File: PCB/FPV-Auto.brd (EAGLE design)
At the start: 65.5 x 30 mm, 93 parts, among them Q310 CSD25402Q3A, Q320 BSS138, U110 NRF24L01+_MINI, U120 74LVC2T45DCT, U140 DRV8835, U200 RASPBERRY_PI_ZERO_W_V1.1_GPIO, U210 MAX98357A, U300 BQ25892, U330 TPS61236P, U340 TPS61236P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

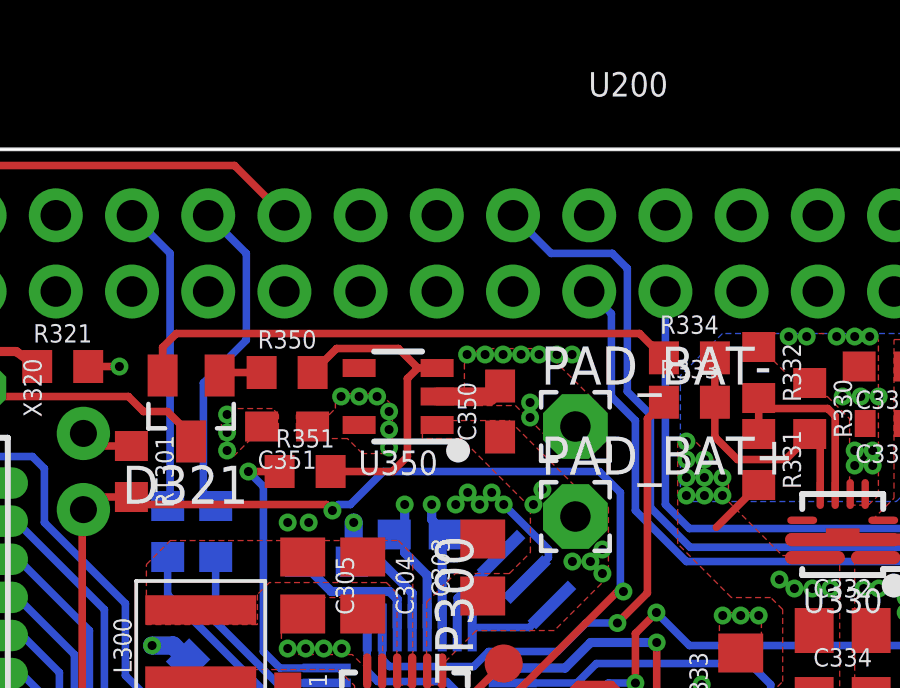
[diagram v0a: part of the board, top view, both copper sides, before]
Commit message: Changes on Raspberry GPIO assignment
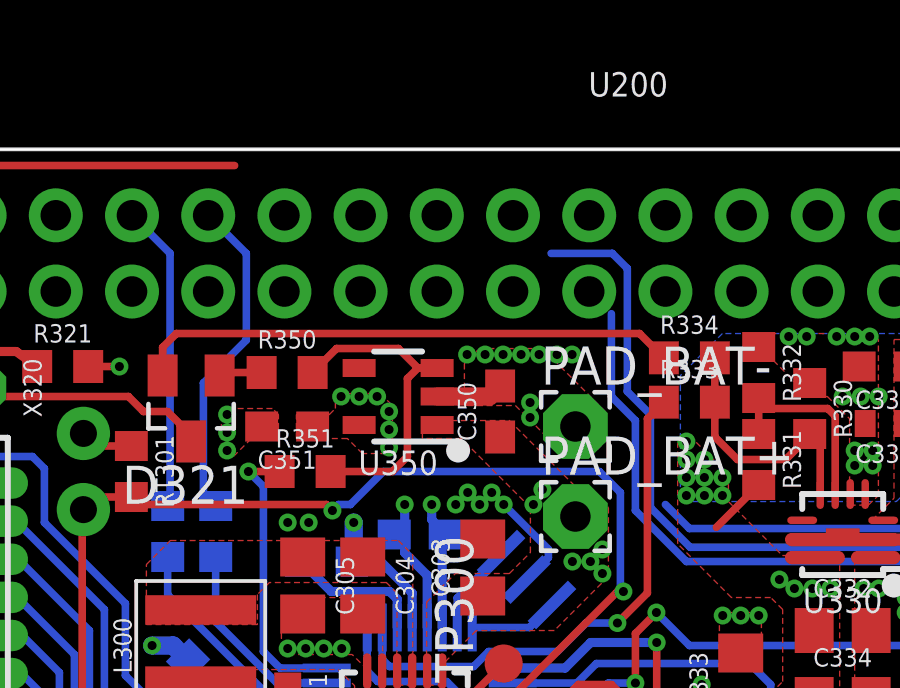
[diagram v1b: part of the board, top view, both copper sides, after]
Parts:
- C212, C213: value 680pF -> 220pF
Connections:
- net BCLK: now also U200.12; no longer U200.18
- net DIN: now also U200.40; no longer U200.21
- net LRCLK: now also U200.35; no longer U200.19
- net RASPI_DTR: now also U200.15; no longer U200.12
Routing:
- net DIN: track 20.1 -> 13.0 mm
- net RASPI_DTR: track 29.6 -> 27.3 mm
- net BCLK: track 30.0 -> 28.2 mm
- net LRCLK: track 26.8 -> 25.7 mm
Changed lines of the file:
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@@
 <grid distance="1" unitdist="mm" unit="mm" style="lines" multiple="1" display="no" altdistance="0.1" altunitdist="mm" altunit="mm"/>
 <layers>
-<layer number="1" name="Top" color="4" fill="1" visible="yes" active="yes"/>
+<layer number="1" name="Top" color="4" fill="1" visible="no" active="yes"/>
 <layer number="2" name="Route2" color="1" fill="3" visible="no" active="yes"/>
 <layer number="3" name="Route3" color="4" fill="3" visible="no" active="no"/>
@@
 <layer number="19" name="Unrouted" color="6" fill="1" visible="yes" active="yes"/>
 <layer number="20" name="Dimension" color="15" fill="1" visible="yes" active="yes"/>
-<layer number="21" name="tPlace" color="7" fill="1" visible="yes" active="yes"/>
+<layer number="21" name="tPlace" color="7" fill="1" visible="no" active="yes"/>
 <layer number="22" name="bPlace" color="7" fill="1" visible="yes" active="yes"/>
 <layer number="23" name="tOrigins" color="15" fill="1" visible="yes" active="yes"/>
@@
 <layer number="49" name="Reference" color="7" fill="1" visible="no" active="yes"/>
 <layer number="50" name="dxf" color="7" fill="1" visible="no" active="no"/>
-<layer number="51" name="tDocu" color="7" fill="1" visible="yes" active="yes"/>
+<layer number="51" name="tDocu" color="7" fill="1" visible="no" active="yes"/>
 <layer number="52" name="bDocu" color="7" fill="1" visible="yes" active="yes"/>
 <layer number="53" name="tGND_GNDA" color="7" fill="1" visible="no" active="no"/>
@@
 <element name="R200" library="FPV-Auto" package="R0603" value="1K" x="17.69" y="17.26" rot="MR270"/>
 <element name="R201" library="FPV-Auto" package="R0603" value="1K" x="19.29" y="17.26" rot="MR270"/>
-<element name="C212" library="FPV-Auto" package="C0603" value="680pF" x="55.99" y="18.36" rot="MR270"/>
-<element name="C213" library="FPV-Auto" package="C0603" value="680pF" x="55.99" y="22.46" rot="MR90"/>
+<element name="C212" library="FPV-Auto" package="C0603" value="220pF" x="55.99" y="18.36" rot="MR270"/>
+<element name="C213" library="FPV-Auto" package="C0603" value="220pF" x="55.99" y="22.46" rot="MR90"/>
 <element name="R211" library="FPV-Auto" package="R0603_SWITCH_2_WAY" value="R_SWITCH_2_WAY_0603" x="44.19" y="18.46" rot="MR180"/>
 <element name="FB210" library="FPV-Auto" package="0603" value="BLM18SG331TN1" x="54.38" y="20.77" rot="MR90">
@@
 </signal>
 <signal name="BCLK">
-<contactref element="U200" pad="18"/>
 <contactref element="U210" pad="16"/>
 <wire x1="30.47" y1="26.53" x2="32.51" y2="26.53" width="0.254" layer="16"/>
 <wire x1="47.74" y1="16.31" x2="47.74" y2="16.735" width="0.254" layer="16"/>
 <wire x1="33.01" y1="26.03" x2="32.51" y2="26.53" width="0.254" layer="16"/>
-<wire x1="30.47" y1="26.53" x2="29.2" y2="27.8" width="0.254" layer="16"/>
 <wire x1="47.74" y1="16.02" x2="47.74" y2="16.735" width="0.254" layer="16"/>
 <wire x1="33.01" y1="26.03" x2="33.01" y2="21.93" width="0.254" layer="16"/>
@@
 <wire x1="44.58" y1="14.56" x2="46.28" y2="14.56" width="0.254" layer="16"/>
 <wire x1="46.28" y1="14.56" x2="47.74" y2="16.02" width="0.254" layer="16"/>
+<contactref element="U200" pad="12"/>
+<wire x1="21.58" y1="27.8" x2="30.47" y2="26.53" width="0" layer="19" extent="16-16"/>
 </signal>
 <signal name="LRCLK">
-<contactref element="U200" pad="19"/>
 <contactref element="U210" pad="14"/>
 <wire x1="48.74" y1="15.61" x2="48.74" y2="16.735" width="0.254" layer="16"/>
@@
 <wire x1="44.38" y1="14.06" x2="47.19" y2="14.06" width="0.254" layer="16"/>
 <wire x1="47.19" y1="14.06" x2="48.74" y2="15.61" width="0.254" layer="16"/>
-<wire x1="31.74" y1="25.26" x2="32.48" y2="24.52" width="0.254" layer="16"/>
 <wire x1="32.48" y1="24.52" x2="32.48" y2="21.76" width="0.254" layer="16"/>
 <wire x1="32.48" y1="21.76" x2="33.28" y2="20.96" width="0.254" layer="16"/>
+<contactref element="U200" pad="35"/>
+<wire x1="48.74" y1="16.735" x2="52.06" y2="25.26" width="0" layer="19" extent="16-16"/>
 </signal>
 <signal name="DIN">
-<contactref element="U200" pad="21"/>
 <contactref element="U210" pad="1"/>
 <wire x1="42.83" y1="17.61" x2="46.865" y2="17.61" width="0.254" layer="16"/>
-<wire x1="34.28" y1="25.26" x2="34.28" y2="18.16" width="0.254" layer="16"/>
 <wire x1="34.28" y1="18.16" x2="35.08" y2="17.36" width="0.254" layer="16"/>
 <wire x1="35.08" y1="17.36" x2="42.58" y2="17.36" width="0.254" layer="16"/>
 <wire x1="42.58" y1="17.36" x2="42.83" y2="17.61" width="0.254" layer="16"/>
+<contactref element="U200" pad="40"/>
+<wire x1="46.865" y1="17.61" x2="57.14" y2="27.8" width="0" layer="19" extent="16-16"/>
 </signal>
 <signal name="GAIN">
@@
 </signal>
 <signal name="RASPI_DTR">
-<contactref element="U200" pad="12"/>
 <contactref element="Q320" pad="2"/>
 <wire x1="2.34" y1="17.56" x2="2.34" y2="18.81" width="0.254" layer="1"/>
@@
 <wire x1="7.49" y1="28.66" x2="8.29" y2="29.46" width="0.254" layer="1"/>
 <wire x1="8.29" y1="29.46" x2="19.92" y2="29.46" width="0.254" layer="1"/>
-<wire x1="19.92" y1="29.46" x2="21.58" y2="27.8" width="0.254" layer="1"/>
+<contactref element="U200" pad="15"/>
+<wire x1="19.92" y1="29.46" x2="26.66" y2="25.26" width="0" layer="19" extent="1-1"/>
 </signal>
 <signal name="AOUT1">

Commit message: Update PCB Layout
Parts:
- added R101: 10K, FPV-Auto:R0603
- added R103: 1K, FPV-Auto:R0603
- R102: value 10K -> 1K
- moved R102 7.48 mm to (20.0, 4.95), flipped to the top, turned to 225 degrees
- moved R300 0.60 mm to (16.8, 2.15)
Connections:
- net +3V3: now also R101.2, R103.2
- net GND: now also U110.9
- net RESET: now also R101.1; no longer R102.1
- net SCL: now also R103.1
- net SDA: now also R102.1
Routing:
- net DIN: track 13.0 -> 46.3 mm
- net LRCLK: track 25.7 -> 14.9 mm, vias 0 -> 1
- net RASPI_DTR: track 27.3 -> 37.2 mm
- net BCLK: track 28.2 -> 37.6 mm
- net RESET: track 45.8 -> 48.4 mm
- net +3V3: track 23.4 -> 25.9 mm, vias 14 -> 15
- net STAT: track 11.1 -> 11.7 mm
- net SDA: track 17.9 -> 18.4 mm
- net SCL: track 15.9 -> 16.5 mm
- net N$19: track 3.99 -> 3.48 mm
- net BAT: vias 21 -> 22

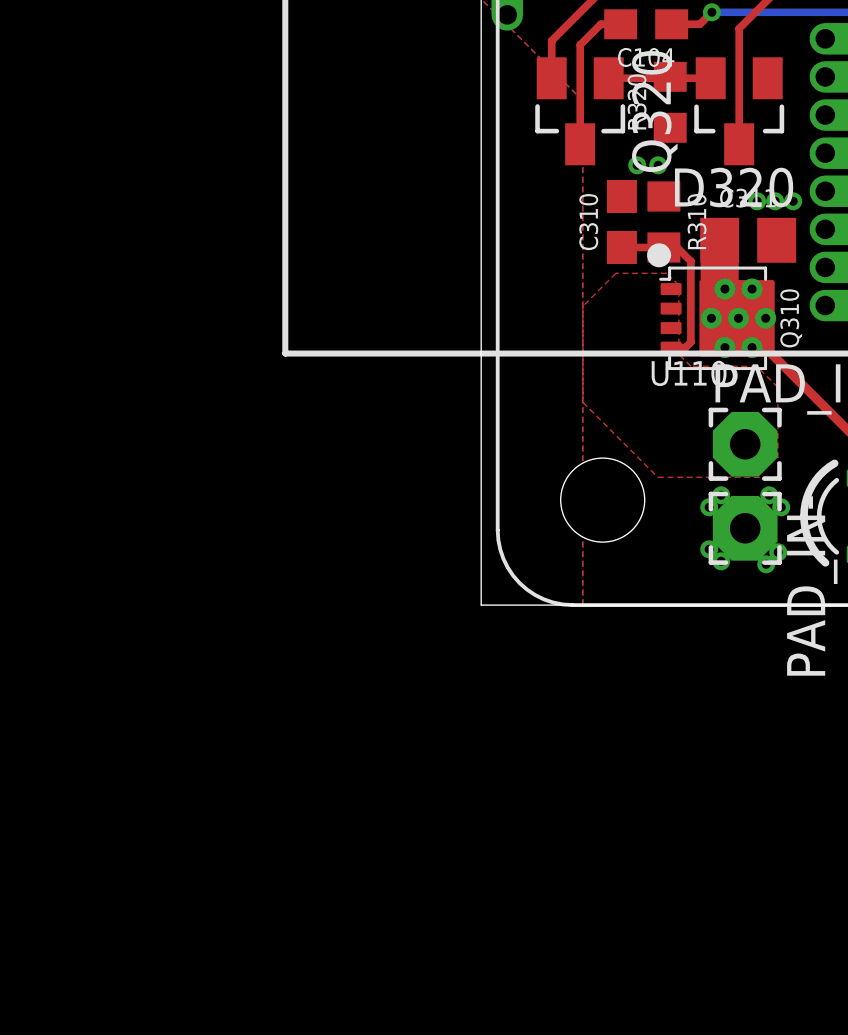
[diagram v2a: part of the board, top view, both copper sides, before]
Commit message: Z-Diode on reverse-prot-mosfet, button also on AVR, other minor changes
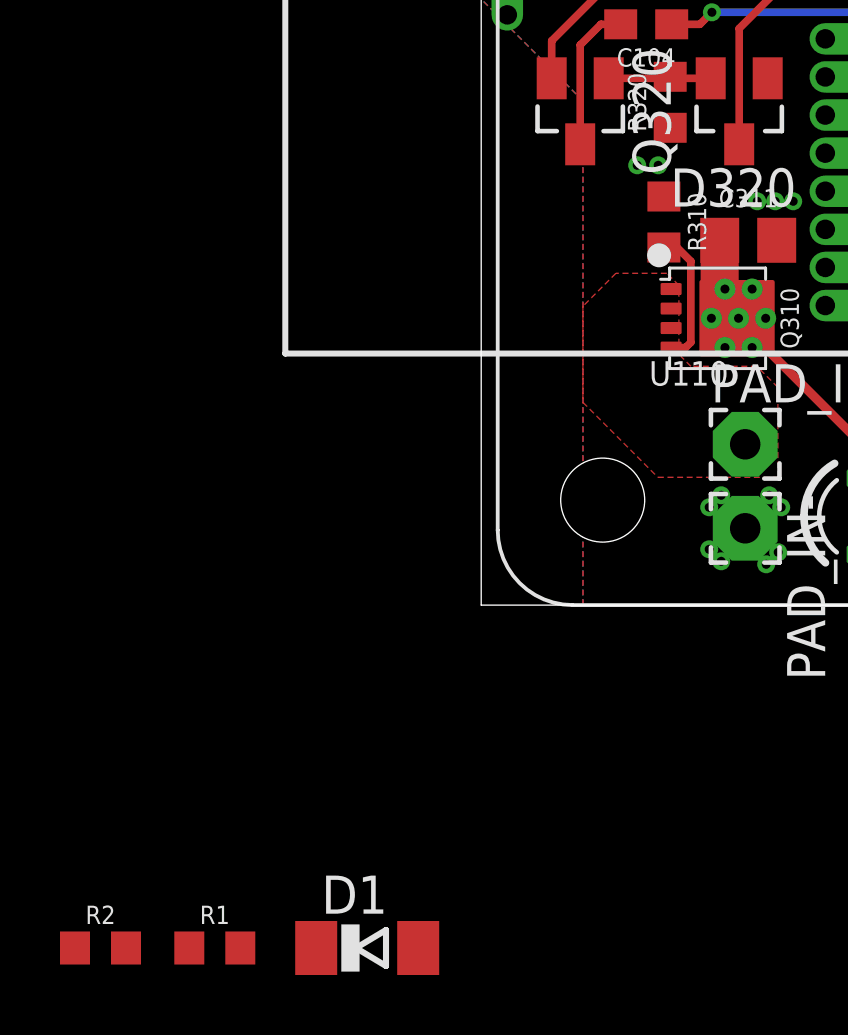
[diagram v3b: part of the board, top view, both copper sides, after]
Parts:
- removed C310: (no value), FPV-Auto:C0603
- added D1: (no value), diode:SOD80C
- added R1, R2: 100K, FPV-Auto:R0603
- R102, R103: value 1K -> 10K
- R310: value 100K -> 10K
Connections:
- new net BUTTON_SENSE: R1.1, R2.2, U100.19
- new net N$15: D320.1, R1.2
- net GND: now also R2.1; no longer C310.2
- net N$16: now also D1.A; no longer C310.1
- net VBUS: now also D1.C
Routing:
- net N$16: track 5.92 -> 4.52 mm

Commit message: updated lib and pcb
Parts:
- removed D1: (no value), diode:SOD80C
- removed R1, R2: 100K, FPV-Auto:R0603
- added D310: BZX585-B9V1, FPV-Auto:SOD523(SC-79)
- added R322, R323: 100K, FPV-Auto:R0603
- U100: value (none) -> ATMEGA328P-AU
- U200: device FPV-Auto:RASPBERRY_PI_ZERO_W_V1.1 -> FPV-Auto:RASPBERRY_PI_ZERO_W_V1.1_GPIO
- moved C311 0.34 mm to (8.91, 12.5)
- moved R310 0.07 mm to (6.10, 12.7)
- flipped U110 to the bottom, turned to 270 degrees
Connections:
- removed net NRF_MISO: U100.26, U110.7
- removed net SCK/NRF_CE: U100.17, U110.3, X100.3
- new net NRF_CE: U100.26, U110.3
- new net SCK/NRF_MISO: U100.17, U110.7, X100.3
- net BUTTON_SENSE: now also R322.1, R323.2, U100.22; no longer R1.1, R2.2, U100.19
- net GND: now also R323.1; no longer R2.1
- net N$15: now also R322.2; no longer R1.2
- net N$16: now also D310.A; no longer D1.A
- net NRF_!CS: now also U100.25; no longer U100.23
- net NRF_MOSI: now also U100.23; no longer U100.25
- net VBUS: now also D310.C; no longer D1.C
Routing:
- net SCK/NRF_MISO: track 0.00 -> 30.5 mm
- net SCK/NRF_CE: track 30.2 -> 0.00 mm
- net NRF_MISO: track 22.1 -> 0.00 mm
- net NRF_CE: track 0.00 -> 20.8 mm
- net N$15: track 0.00 -> 18.7 mm, vias 0 -> 1
- net BUTTON_SENSE: track 0.00 -> 12.4 mm
- net VBUS: track 11.4 -> 16.5 mm
- net N$16: track 4.52 -> 6.59 mm
- net NRF_!CS: track 21.7 -> 20.0 mm
- net NRF_SCK: track 21.2 -> 20.0 mm
- net GND: track 43.7 -> 44.6 mm, vias 109 -> 108
- net NRF_MOSI: track 21.2 -> 20.4 mm

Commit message: Kommentare...
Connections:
- removed net STAT: R300.1, U300.4
- new net N$20: LED300.A, LED301.A, R300.1
- net N$19: now also U300.4; no longer R300.2
- net VBUS: now also R300.2; no longer LED300.A, LED301.A
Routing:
- net STAT: track 12.0 -> 0.00 mm, vias 2 -> 0
- net VBUS: track 16.5 -> 13.5 mm
- net N$20: track 0.00 -> 2.03 mm
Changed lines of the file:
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@@
 <layers>
 <layer number="1" name="Top" color="4" fill="1" visible="yes" active="yes"/>
-<layer number="2" name="Route2" color="1" fill="3" visible="no" active="yes"/>
+<layer number="2" name="Route2" color="3" fill="1" visible="no" active="yes"/>
 <layer number="3" name="Route3" color="4" fill="3" visible="no" active="no"/>
 <layer number="14" name="Route14" color="1" fill="6" visible="no" active="no"/>
-<layer number="15" name="Route15" color="4" fill="6" visible="no" active="yes"/>
-<layer number="16" name="Bottom" color="1" fill="1" visible="yes" active="yes"/>
+<layer number="15" name="Route15" color="5" fill="1" visible="no" active="yes"/>
+<layer number="16" name="Bottom" color="1" fill="1" visible="no" active="yes"/>
 <layer number="17" name="Pads" color="2" fill="1" visible="yes" active="yes"/>
 <layer number="18" name="Vias" color="2" fill="1" visible="yes" active="yes"/>
@@
 <layer number="20" name="Dimension" color="15" fill="1" visible="yes" active="yes"/>
 <layer number="21" name="tPlace" color="7" fill="1" visible="yes" active="yes"/>
-<layer number="22" name="bPlace" color="7" fill="1" visible="yes" active="yes"/>
+<layer number="22" name="bPlace" color="7" fill="1" visible="no" active="yes"/>
 <layer number="23" name="tOrigins" color="15" fill="1" visible="yes" active="yes"/>
-<layer number="24" name="bOrigins" color="15" fill="1" visible="yes" active="yes"/>
+<layer number="24" name="bOrigins" color="15" fill="1" visible="no" active="yes"/>
 <layer number="25" name="tNames" color="7" fill="1" visible="no" active="yes"/>
 <layer number="26" name="bNames" color="7" fill="1" visible="no" active="yes"/>
 <layer number="27" name="tValues" color="7" fill="1" visible="no" active="yes"/>
 <layer number="28" name="bValues" color="7" fill="1" visible="no" active="yes"/>
-<layer number="29" name="tStop" color="7" fill="3" visible="no" active="yes"/>
+<layer number="29" name="tStop" color="7" fill="3" visible="yes" active="yes"/>
 <layer number="30" name="bStop" color="7" fill="6" visible="no" active="yes"/>
 <layer number="31" name="tCream" color="7" fill="4" visible="no" active="yes"/>
@@
 <layer number="50" name="dxf" color="7" fill="1" visible="no" active="no"/>
 <layer number="51" name="tDocu" color="7" fill="1" visible="yes" active="yes"/>
-<layer number="52" name="bDocu" color="7" fill="1" visible="yes" active="yes"/>
+<layer number="52" name="bDocu" color="7" fill="1" visible="no" active="yes"/>
 <layer number="53" name="tGND_GNDA" color="7" fill="1" visible="no" active="no"/>
 <layer number="54" name="bGND_GNDA" color="7" fill="1" visible="no" active="no"/>
@@
 <contactref element="Q310" pad="TP2" route="any" routetag="A.S"/>
 <contactref element="C311" pad="1"/>
-<contactref element="LED300" pad="A"/>
 <via x="23.7" y="8.6" extent="1-16" drill="0.3"/>
 <via x="23.7" y="8" extent="1-16" drill="0.3"/>
@@
 <via x="23.1" y="8" extent="1-16" drill="0.3"/>
 <via x="23.1" y="7.4" extent="1-16" drill="0.3"/>
-<contactref element="LED301" pad="A"/>
-<wire x1="12.8" y1="4.27" x2="13.32" y2="3.75" width="0.254" layer="1"/>
-<wire x1="13.32" y1="3.75" x2="14.61" y2="3.75" width="0.254" layer="1"/>
 <wire x1="7.96" y1="12.5" x2="7.96" y2="12" width="1.27" layer="1"/>
 <wire x1="7.96" y1="12" x2="7.96" y2="9.6" width="1.27" layer="1"/>
 <wire x1="7.96" y1="9.6" x2="8.5875" y2="9.6" width="1.27" layer="1"/>
-<wire x1="12.8" y1="4.27" x2="12.8" y2="5.3" width="0.3048" layer="1"/>
 <wire x1="12.8" y1="5.3" x2="9.475" y2="8.625" width="0.3048" layer="1"/>
 <wire x1="9.475" y1="8.625" x2="9.04" y2="8.625" width="0.3048" layer="1"/>
@@
 <wire x1="4.7" y1="12.7" x2="7.96" y2="12.7" width="0.254" layer="1"/>
 <wire x1="7.96" y1="12.7" x2="7.96" y2="12" width="0.254" layer="1"/>
+<contactref element="R300" pad="2"/>
+<wire x1="12.8" y1="5.3" x2="15.95" y2="2.19" width="0" layer="19" extent="1-1"/>
 </signal>
 <signal name="N$17">
@@
 </polygon>
 </signal>
-<signal name="STAT">
-<contactref element="U300" pad="4"/>
-<contactref element="R300" pad="1"/>
-<wire x1="25.86" y1="8.355" x2="25.86" y2="7.56" width="0.254" layer="1"/>
-<wire x1="25.86" y1="7.56" x2="24.2" y2="5.9" width="0.254" layer="1"/>
-<via x="24.2" y="4.6" extent="1-16" drill="0.3"/>
-<wire x1="24.2" y1="5.9" x2="24.2" y2="4.6" width="0.254" layer="1"/>
-<via x="18.7" y="2.2" extent="1-16" drill="0.3"/>
-<wire x1="18.7" y1="2.2" x2="18.69" y2="2.19" width="0.254" layer="1"/>
-<wire x1="18.69" y1="2.19" x2="17.65" y2="2.19" width="0.254" layer="1"/>
-<wire x1="18.7" y1="2.2" x2="21.8" y2="2.2" width="0.254" layer="16"/>
-<wire x1="21.8" y1="2.2" x2="24.2" y2="4.6" width="0.254" layer="16"/>
-</signal>
 <signal name="N$19">
-<contactref element="R300" pad="2"/>
 <contactref element="LED300" pad="C"/>
 <contactref element="LED301" pad="K"/>
-<wire x1="15.95" y1="2.19" x2="15.99" y2="2.25" width="0.254" layer="1"/>
 <wire x1="15.99" y1="2.25" x2="14.61" y2="2.25" width="0.254" layer="1"/>
 <wire x1="12.8" y1="1.73" x2="13.32" y2="2.25" width="0.254" layer="1"/>
 <wire x1="13.32" y1="2.25" x2="14.61" y2="2.25" width="0.254" layer="1"/>
+<contactref element="U300" pad="4"/>
+<wire x1="15.99" y1="2.25" x2="25.86" y2="8.355" width="0" layer="19" extent="1-1"/>
 </signal>
 <signal name="EN_5V1">
@@
 <wire x1="16.772759375" y1="4.172753125" x2="15.758615625" y2="5.186896875" width="0.254" layer="16"/>
 </signal>
+<signal name="N$20">
+<contactref element="LED300" pad="A"/>
+<contactref element="LED301" pad="A"/>
+<wire x1="12.8" y1="4.27" x2="13.32" y2="3.75" width="0.254" layer="1"/>
+<wire x1="13.32" y1="3.75" x2="14.61" y2="3.75" width="0.254" layer="1"/>
+<contactref element="R300" pad="1"/>
+<wire x1="17.65" y1="2.19" x2="14.61" y2="3.75" width="0" layer="19" extent="1-1"/>
+</signal>
 </signals>
